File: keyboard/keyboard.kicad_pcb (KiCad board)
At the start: 2 copper layers, 69 parts, among them J1 TYPE-C-31-M-12, J2 Conn_01x03_Socket, J3 Conn_01x02_Pin, J4 AudioJack4, J5 Conn_02x06_Top_Bottom, J6 Conn_02x06_Top_Bottom, J7 Conn_01x05_Socket, SW1 SW_MEC_5G, SW10 SW_MEC_5G, SW11 SW_MEC_5G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

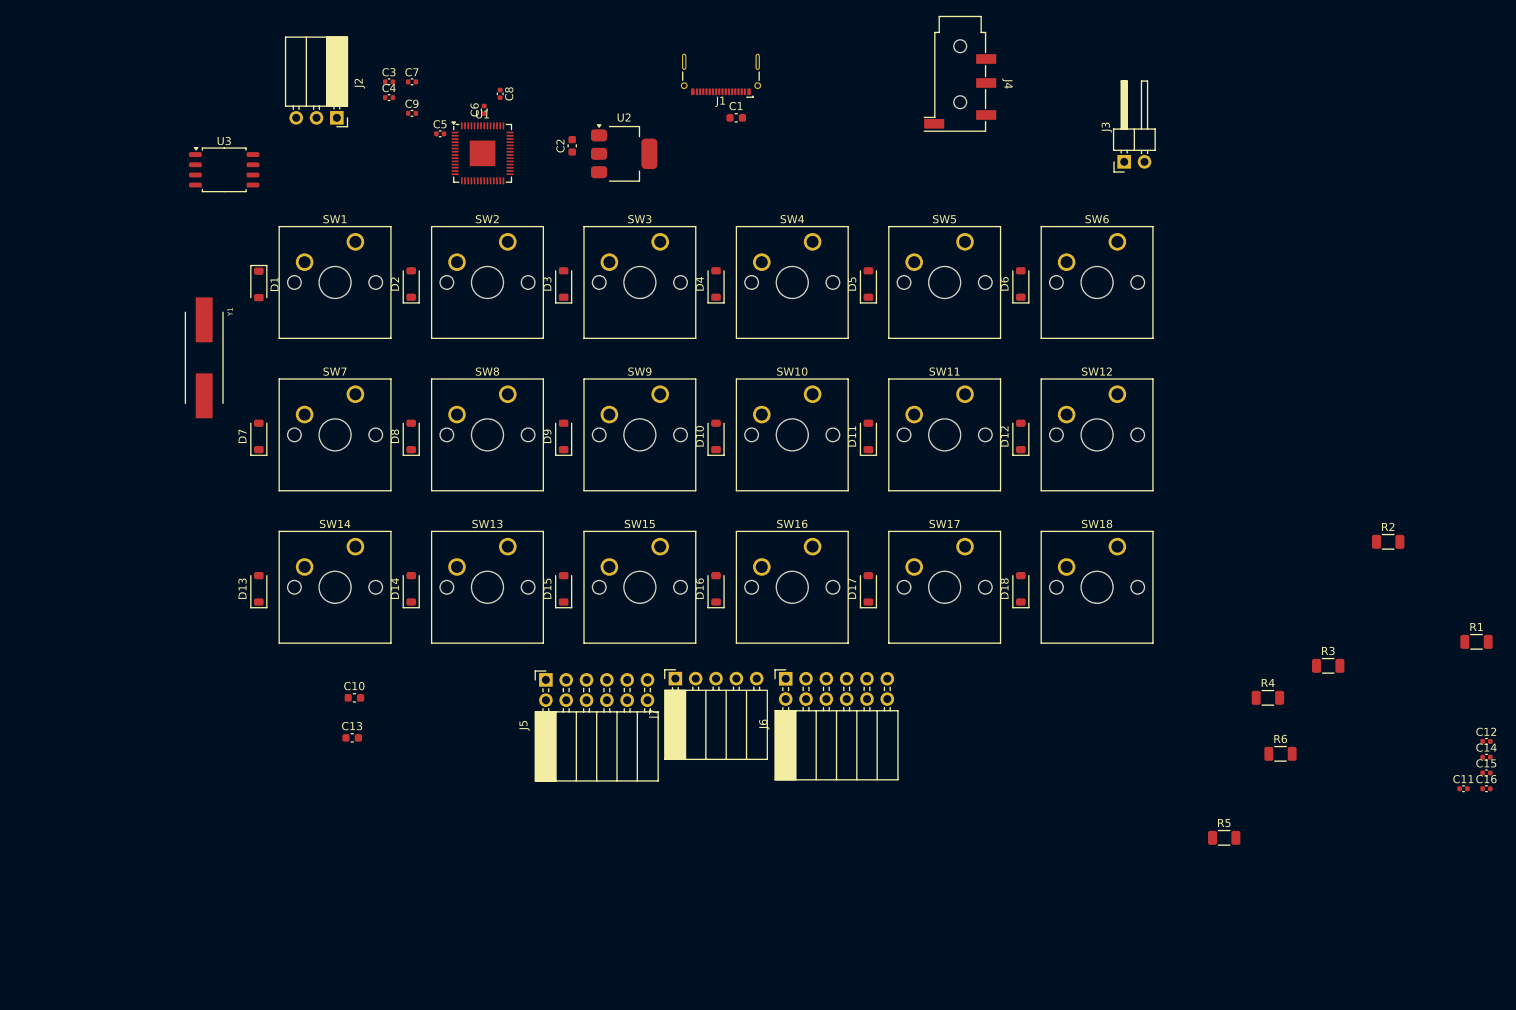
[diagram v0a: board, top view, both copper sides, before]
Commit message: add footprints and New design as BOARD
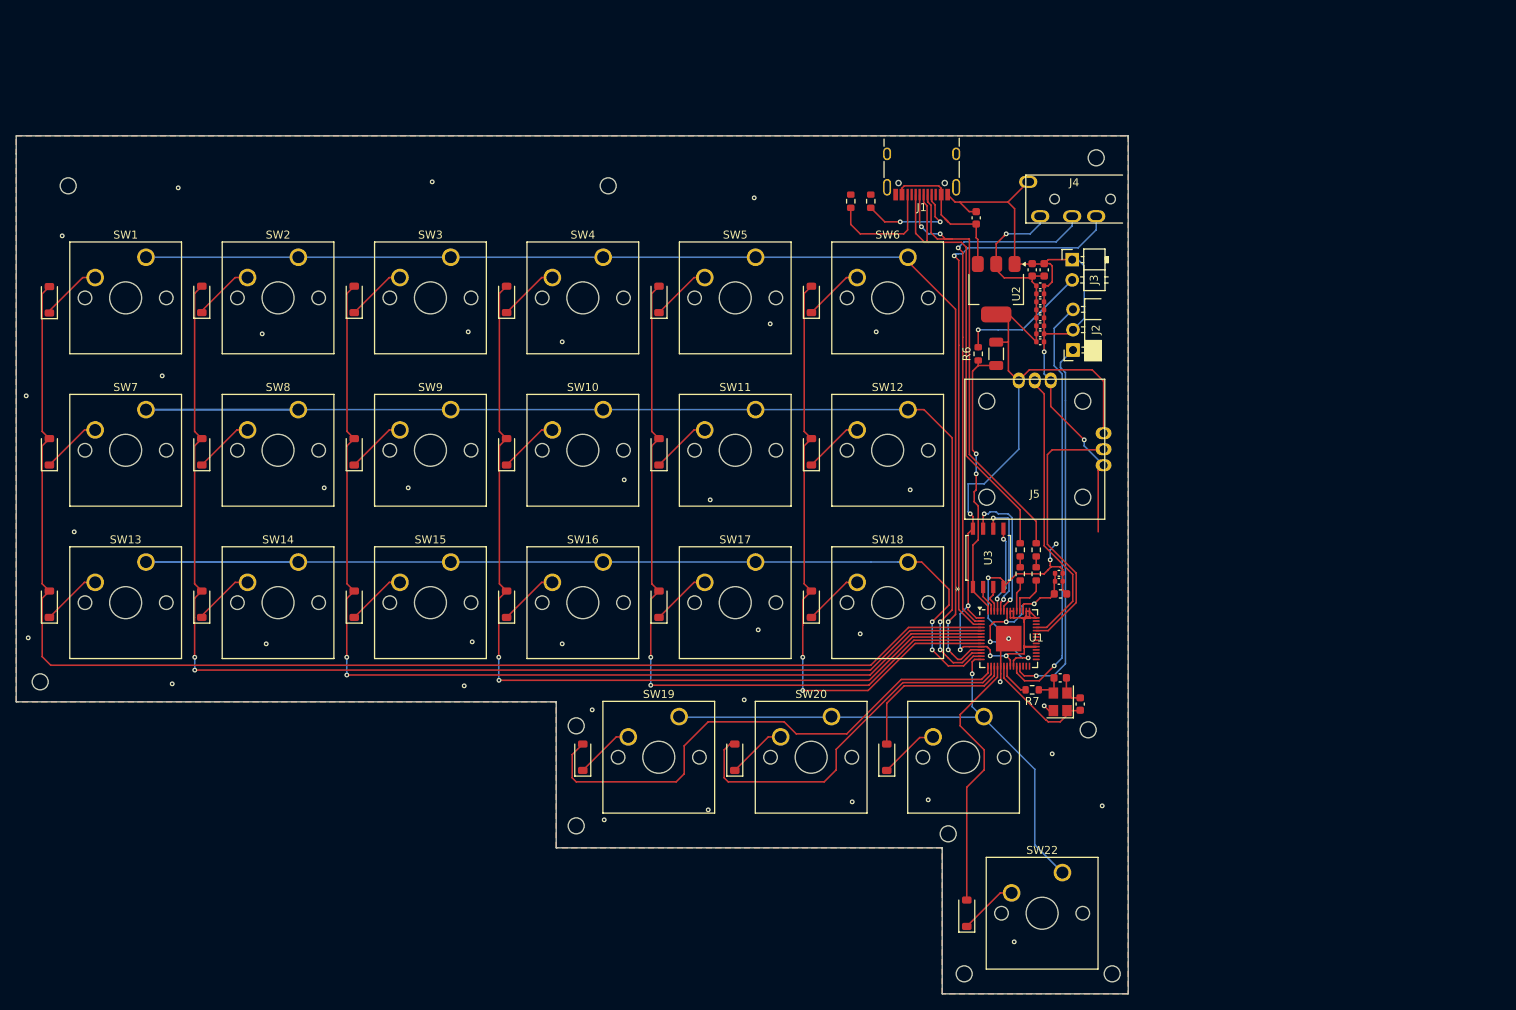
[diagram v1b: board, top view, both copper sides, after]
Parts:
- removed J6: Conn_02x06_Top_Bottom, Connector_PinSocket_2.54mm:PinSocket_2x06_P2.54mm_Horizontal
- removed J7: Conn_01x05_Socket, Connector_PinSocket_2.54mm:PinSocket_1x05_P2.54mm_Horizontal
- added D19: D, Diode_SMD:D_SOD-123, F.Cu at (143.3, 121.9)
- added D20: D, Diode_SMD:D_SOD-123, F.Cu at (162.3, 121.9)
- added D21: D, Diode_SMD:D_SOD-123, F.Cu at (181.3, 121.9)
- added D22: D, Diode_SMD:D_SOD-123, F.Cu at (191.3, 141.4)
- added R7: 1K, Resistor_SMD:R_0603_1608Metric, F.Cu at (199.5, 113.5)
- added R8: 22, Resistor_SMD:R_0603_1608Metric, F.Cu at (198.0, 99.0)
- added R9: 22, Resistor_SMD:R_0603_1608Metric, F.Cu at (200.0, 99.0)
- added SW19: SW_MEC_5G, Button_Switch_Keyboard:SW_Cherry_MX_1.00u_PCB, F.Cu at (155.4, 116.8)
- added SW20: SW_MEC_5G, Button_Switch_Keyboard:SW_Cherry_MX_1.00u_PCB, F.Cu at (174.4, 116.8)
- added SW21: SW_MEC_5G, Button_Switch_Keyboard:SW_Cherry_MX_1.00u_PCB, F.Cu at (193.5, 116.8)
- added SW22: SW_MEC_5G, Button_Switch_Keyboard:SW_Cherry_MX_1.00u_PCB, F.Cu at (203.3, 136.3)
- C15, C16: value 27p -> 30p; footprint Capacitor_SMD:C_0402_1005Metric -> Capacitor_SMD:C_0603_1608Metric
- J1: footprint Connector_USB:USB_C_Receptacle_G-Switch_GT-USB-7025 -> Connector_USB:USB_C_Receptacle_HRO_TYPE-C-31-M-12
- J2: footprint Connector_PinSocket_2.54mm:PinSocket_1x03_P2.54mm_Horizontal -> footprint:PinSocket_1x03_P2.54mm_Horizontal
- J3: footprint Connector_PinHeader_2.54mm:PinHeader_1x02_P2.54mm_Horizontal -> footprint:PinHeader_1x02_P2.54mm_Horizontal
- J4: footprint Connector_Audio:Jack_3.5mm_KoreanHropartsElec_PJ-320D-4A_Horizontal -> footprint:MJ-4PP-9
- J5: value Conn_02x06_Top_Bottom -> Conn_01x04_Socket; footprint Connector_PinSocket_2.54mm:PinSocket_2x06_P2.54mm_Horizontal -> footprint:JT8P-3.2T- -1-16Y
- R1, R2, R6: footprint Resistor_SMD:R_1206_3216Metric -> Resistor_SMD:R_0603_1608Metric
- R3, R4: value 27.4 -> 5.1; footprint Resistor_SMD:R_1206_3216Metric -> Resistor_SMD:R_0603_1608Metric
- U3: footprint Package_SO:SOIC-8_5.23x5.23mm_P1.27mm -> footprint:SOIC_128JVSIM_WIN
- Y1: value ABLS-12.000MHZ-B4-T -> Crystal_GND23; footprint kicad:XTAL_ABLS-27.120MHZ-B4-F-T -> Crystal:Crystal_SMD_3225-4Pin_3.2x2.5mm
- moved Y1 115.3 mm to (203.0, 115.0), turned to 90 degrees
- moved U3 107.1 mm to (194.0, 97.0), turned to 90 degrees
- moved C10 101.5 mm to (201.0, 61.0), turned to 90 degrees
- moved J2 96.5 mm to (204.6, 71.0), turned to 180 degrees
- moved R1 93.6 mm to (179.3, 52.4), turned to -90 degrees
- moved C13 90.3 mm to (203.0, 101.5)
- moved U1 89.5 mm to (196.6, 107.1)
- moved C4 85.9 mm to (200.5, 67.0)
- moved C3 85.3 mm to (200.5, 63.0)
- moved C7 83.2 mm to (200.5, 65.0)
- moved C9 81.7 mm to (200.5, 64.0)
- moved R2 79.5 mm to (176.8, 52.4), turned to -90 degrees
- moved C5 79.4 mm to (200.5, 70.0)
- moved C14 79.0 mm to (200.5, 66.0)
- moved C6 74.9 mm to (200.5, 69.0), turned to 0 degrees
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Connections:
- C16 pad 2: XOUT -> Net-(C16-Pad2)
- D10 pad 2: col5 -> col4
- D11 pad 2: col1 -> col5
- D12 pad 2: col2 -> col6
- D13 pad 2: col3 -> col1
- D14 pad 2: col4 -> col2
- D15 pad 2: col5 -> col3
- D16 pad 2: col6 -> col4
- D17 pad 2: col6 -> col5
- D6 pad 2: col1 -> col6
- D7 pad 2: col2 -> col1
- D8 pad 2: col3 -> col2
- D9 pad 2: col4 -> col3
- J5 pad 1: GPIO23 -> GND
- J5 pad 2: GPIO21 -> GPIO27
- J5 pad 3: GPIO19 -> +3.3V
- J5 pad 4: GPIO17 -> GPIO26
- R3 pad 1: USB_DM -> Net-(R3-Pad1)
- R4 pad 1: USB_DP -> Net-(R4-Pad1)
- SW10 pad 2: Net-(D9-K) -> Net-(D10-K)
- SW11 pad 2: Net-(D10-K) -> Net-(D11-K)
- SW12 pad 2: Net-(D17-K) -> Net-(D12-K)
- SW13 pad 2: Net-(D11-K) -> Net-(D13-K)
- SW14 pad 2: Net-(D12-K) -> Net-(D14-K)
- SW15 pad 2: Net-(D13-K) -> Net-(D15-K)
- SW16 pad 2: Net-(D14-K) -> Net-(D16-K)
- SW17 pad 2: Net-(D15-K) -> Net-(D17-K)
- SW6 pad 2: Net-(D16-K) -> Net-(D6-K)
- SW7 pad 2: Net-(D6-K) -> Net-(D7-K)
- SW8 pad 2: Net-(D7-K) -> Net-(D8-K)
- SW9 pad 2: Net-(D8-K) -> Net-(D9-K)
- U1 pad 14: GPIO11 -> rowX
- U1 pad 15: GPIO12 -> colX1
- U1 pad 16: GPIO13 -> colX2
- U1 pad 17: GPIO14 -> colX3
- U1 pad 18: GPIO15 -> colX4
- Y1 pad 1: XOUT -> XIN
- Y1 pad 2: XIN -> GND
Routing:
- net col1: track 0.00 -> 167.9 mm
- net row2: track 0.00 -> 154.7 mm, vias 0 -> 2
- net row1: track 0.00 -> 152.3 mm, vias 0 -> 2
- net col2: track 0.00 -> 150.2 mm, vias 0 -> 2
- net row3: track 0.00 -> 138.0 mm, vias 0 -> 2
- net col3: track 0.00 -> 131.9 mm, vias 0 -> 2
- net +3.3V: track 0.00 -> 130.5 mm, vias 0 -> 6
- net GND: track 0.00 -> 121.4 mm, vias 0 -> 42
- net col4: track 0.00 -> 113.7 mm, vias 0 -> 2
- net col5: track 0.00 -> 95.4 mm, vias 0 -> 2
- net col6: track 0.00 -> 77.2 mm, vias 0 -> 2
- net rowX: track 0.00 -> 70.3 mm, vias 0 -> 1
- net GPIO1: track 0.00 -> 68.8 mm, vias 0 -> 1
- net colX1: track 0.00 -> 66.7 mm
- net GPIO0: track 0.00 -> 64.9 mm, vias 0 -> 1
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- added copper zone on B.Cu, net GND
- added copper zone on F.Cu, net GND
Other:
- board outline added: 139 x 107.2 mm
